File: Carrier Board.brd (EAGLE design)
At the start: 90 x 38.6 mm, 55 parts, among them J1 H4P-SMD-2.0, J2 H4P-SMD-2.0, J4 S2B-PH-SM4-TB(LF)(SN), J5 S2B-PH-SM4-TB(LF)(SN), Q1 MMBT2222A, SW2 MF-SW-TACT-6MM, U1 TMP36GRTZ, U2 TPL5010, U3 MB85RC64, U7 NAND

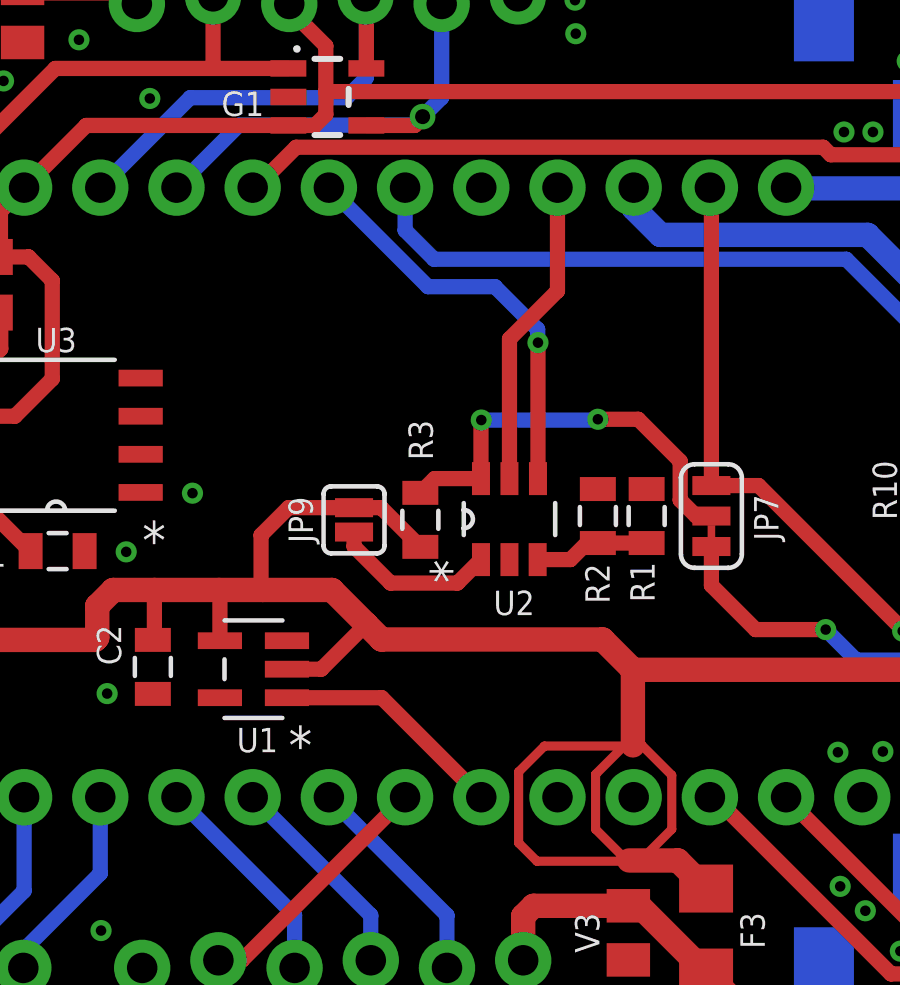
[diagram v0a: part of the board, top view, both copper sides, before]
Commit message: Had to move the Done pin to A3
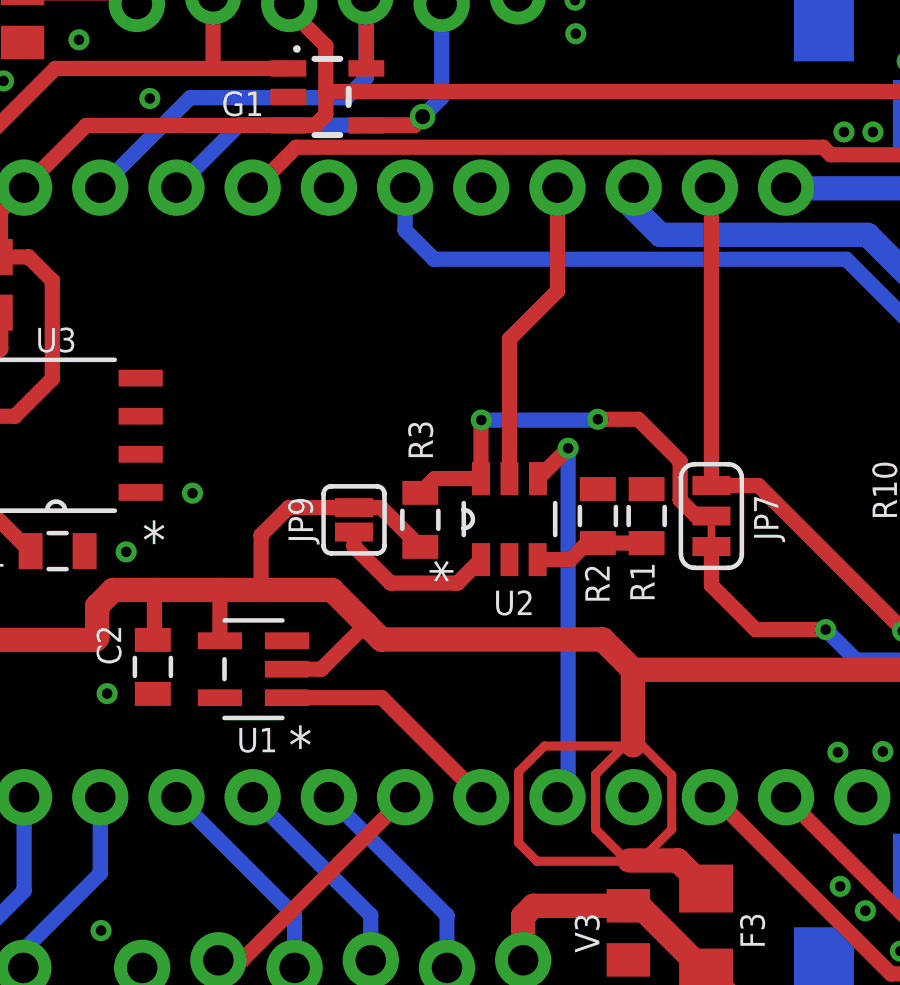
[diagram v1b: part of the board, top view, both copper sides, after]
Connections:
- removed net A3: BORON/ARGON/XENON.A3
- net DONE: now also BORON/ARGON/XENON.A3; no longer BORON/ARGON/XENON.D5
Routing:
- net DONE: track 13.9 -> 13.2 mm
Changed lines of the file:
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@@
 <?xml version="1.0" encoding="utf-8"?>
 <!DOCTYPE eagle SYSTEM "eagle.dtd">
-<eagle version="9.3.2">
+<eagle version="9.4.0">
 <drawing>
 <settings>
@@
 <wire x1="10.490196875" y1="9.220196875" x2="10.4902" y2="9.2202" width="0.508" layer="16"/>
 </signal>
-<signal name="A3">
-<contactref element="BORON/ARGON/XENON" pad="A3"/>
-</signal>
 <signal name="A2">
 <contactref element="BORON/ARGON/XENON" pad="A2"/>
@@
 <signal name="DONE">
 <contactref element="U2" pad="4"/>
-<contactref element="BORON/ARGON/XENON" pad="D5"/>
-<wire x1="27.62" y1="24.3728" x2="27.62" y2="19.8412" width="0.508" layer="1"/>
-<wire x1="20.6502" y1="29.5402" x2="23.9522" y2="26.2382" width="0.508" layer="16"/>
-<wire x1="23.9522" y1="26.2382" x2="26.1874" y2="26.2382" width="0.508" layer="16"/>
-<wire x1="26.1874" y1="26.2382" x2="27.6098" y2="24.8158" width="0.508" layer="16"/>
-<wire x1="27.6098" y1="24.8158" x2="27.6098" y2="24.3626" width="0.508" layer="16"/>
-<wire x1="27.6098" y1="24.3626" x2="27.62" y2="24.3728" width="0.508" layer="16"/>
-<via x="27.62" y="24.3728" extent="1-16" drill="0.35"/>
+<contactref element="BORON/ARGON/XENON" pad="A3"/>
+<wire x1="27.62" y1="19.8412" x2="28.6068" y2="20.828" width="0.508" layer="1"/>
+<wire x1="28.6068" y1="20.828" x2="28.6258" y2="20.828" width="0.508" layer="1"/>
+<wire x1="28.6258" y1="20.828" x2="28.6258" y2="20.8534" width="0.508" layer="1"/>
+<via x="28.6258" y="20.8534" extent="1-16" drill="0.35"/>
+<wire x1="28.6258" y1="20.8534" x2="28.6258" y2="9.5758" width="0.508" layer="16"/>
+<wire x1="28.6258" y1="9.5758" x2="28.2702" y2="9.2202" width="0.508" layer="16"/>
 </signal>
 <signal name="RX">
